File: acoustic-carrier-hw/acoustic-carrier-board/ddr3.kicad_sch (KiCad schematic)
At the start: 21 parts, among them IC1101 MT41K256M16TW-107_P

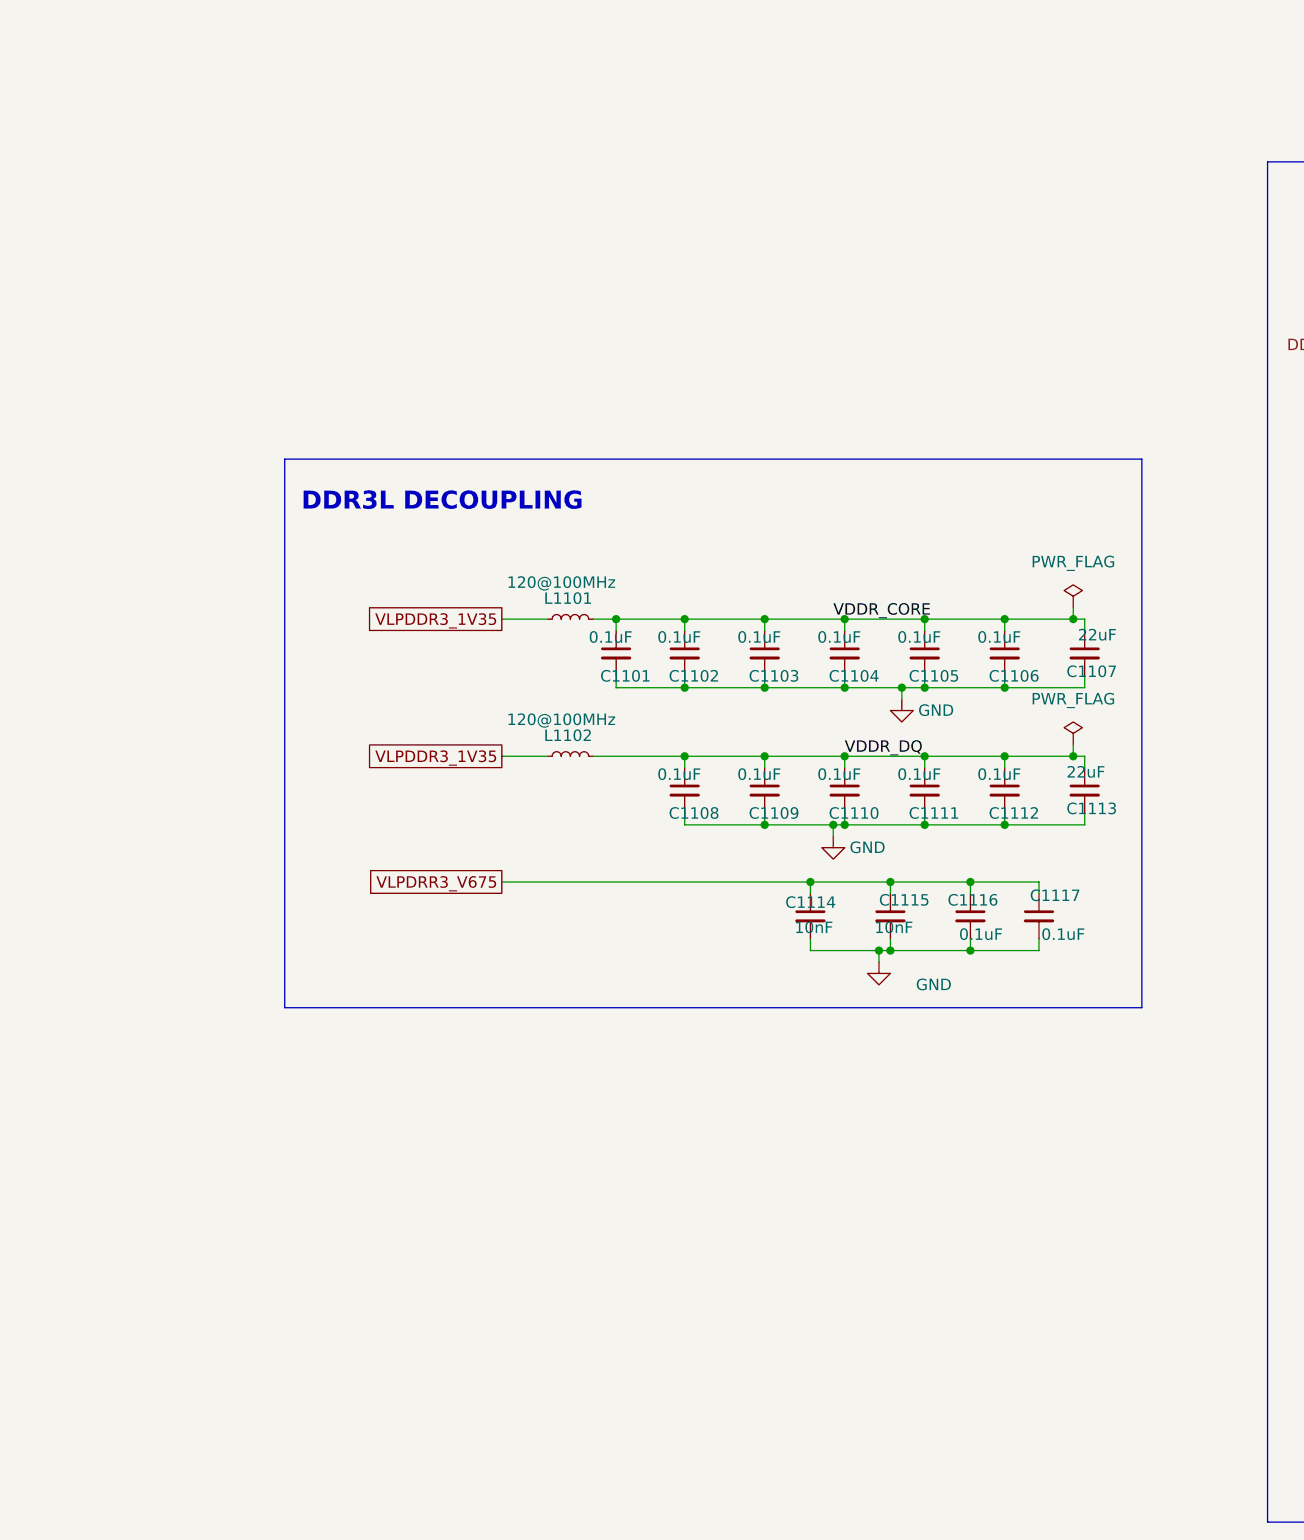
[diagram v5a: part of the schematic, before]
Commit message: [carrier] Removed USB-switch, placed decouplpling for DDR3 and ECP5U (next) consider adding buffers on CC1 and CC2 pins
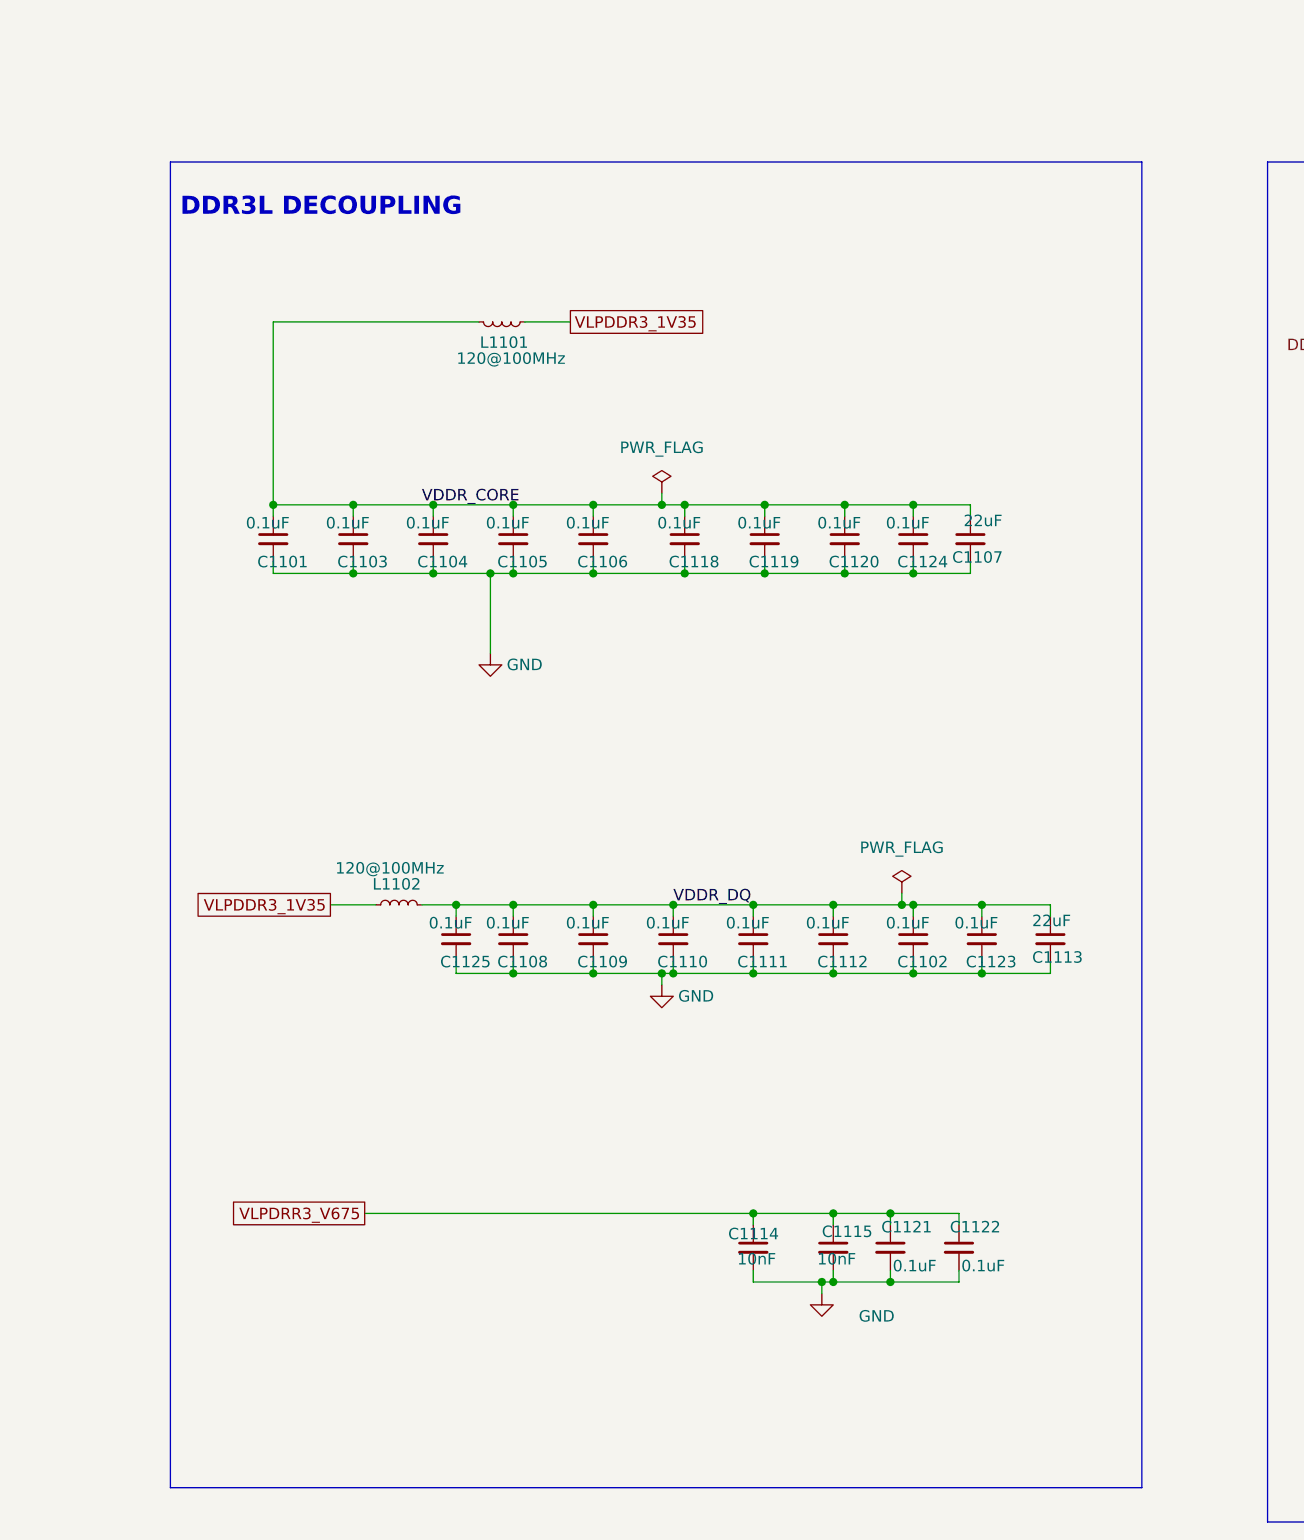
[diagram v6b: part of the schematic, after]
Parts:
- removed C1116, C1117: 0.1uF, Capacitor_SMD:C_0402_1005Metric, symbol Device:C_Small
- added C1118, C1119, C1120, C1121, C1122, C1123, C1124, C1125: 0.1uF, Capacitor_SMD:C_0201_0603Metric, symbol Device:C_Small
- C1101, C1102, C1103, C1104, C1105, C1106, C1108, C1109, C1110, C1111, C1112: footprint Capacitor_SMD:C_0402_1005Metric -> Capacitor_SMD:C_0201_0603Metric; LPN C307331 -> C22435929; MPN CL05B104KB54PNC -> CGA0201X7R104K160ET
- C1114, C1115: footprint Capacitor_SMD:C_0402_1005Metric -> Capacitor_SMD:C_0201_0603Metric; LPN C15195 -> C285010; MPN CL05B103KB5NNNC -> 0201B103K250NT
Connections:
- net GND: now also C1118.2, C1119.2, C1120.2, C1121.2, C1122.2, C1123.2, C1124.2, C1125.2
- net VDDR_CORE: now also C1118.1, C1119.1, C1120.1, C1124.1; no longer C1102.1
- net VDDR_DQ: now also C1102.1, C1123.1, C1125.1
- net VLPDRR3_V675: now also C1121.1, C1122.1
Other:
- moved on the sheet: C1101, C1103, C1104, C1105, C1106, C1107, C1108, C1109, C1110, C1111, C1112, C1113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

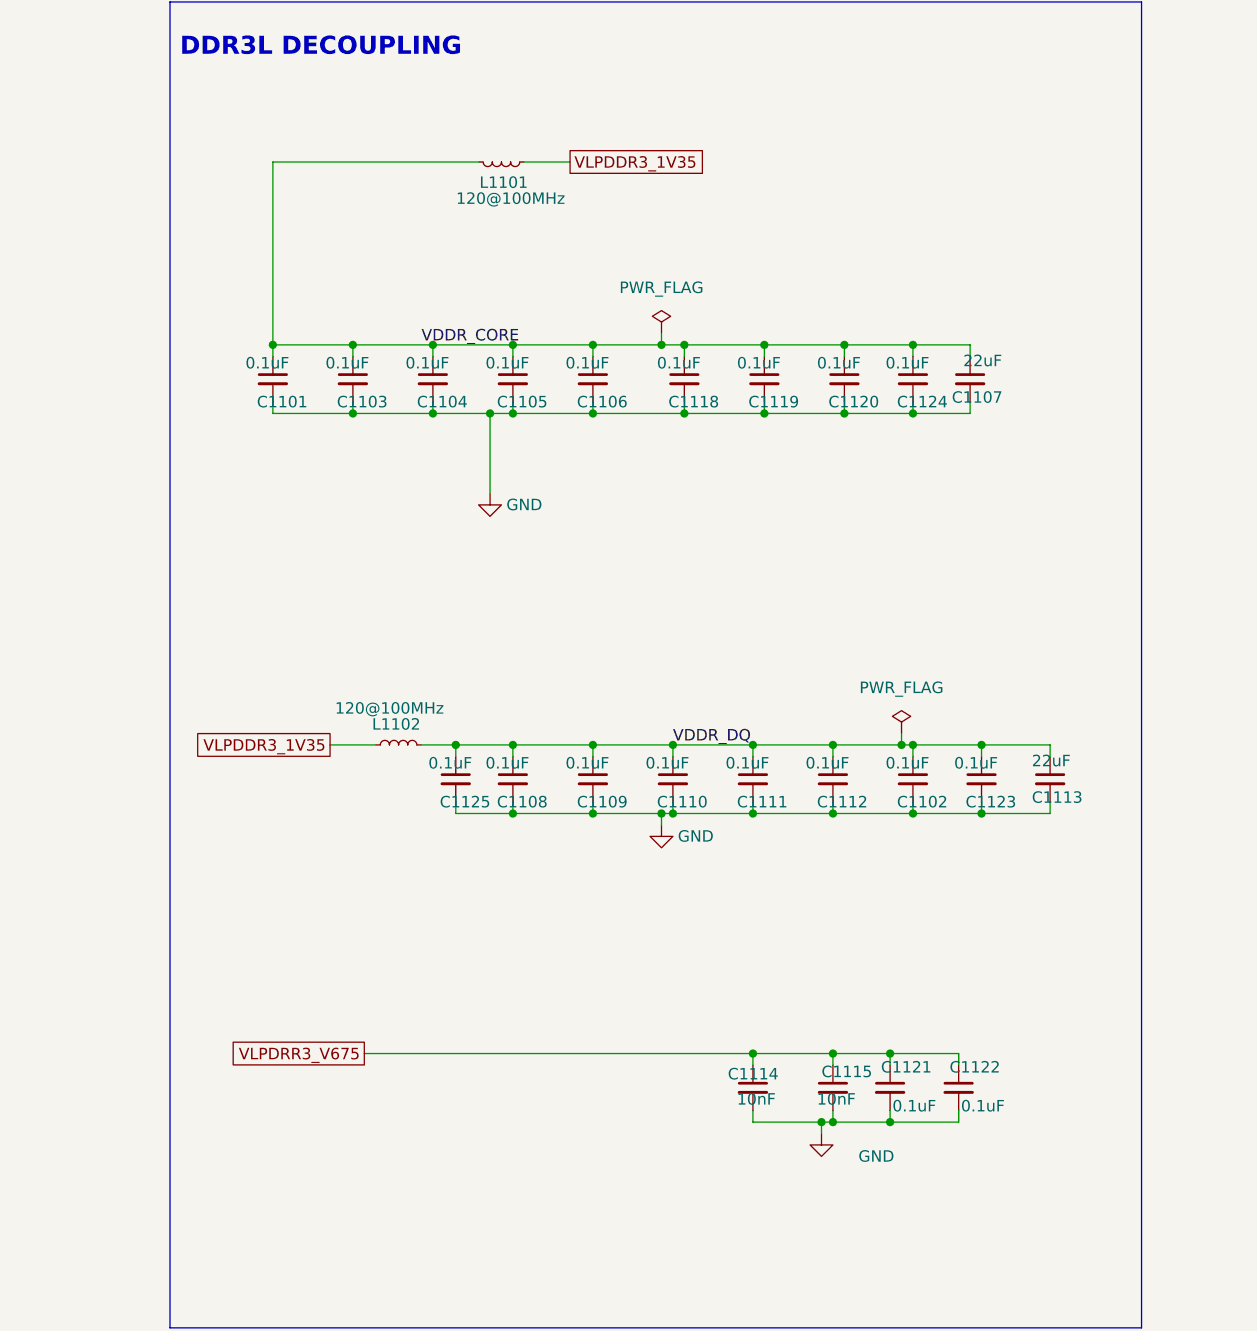
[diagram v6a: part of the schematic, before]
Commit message: [carrier] connected ethernet, usb and adc to appropriate banks, redpositioned schmitt trigger and USB
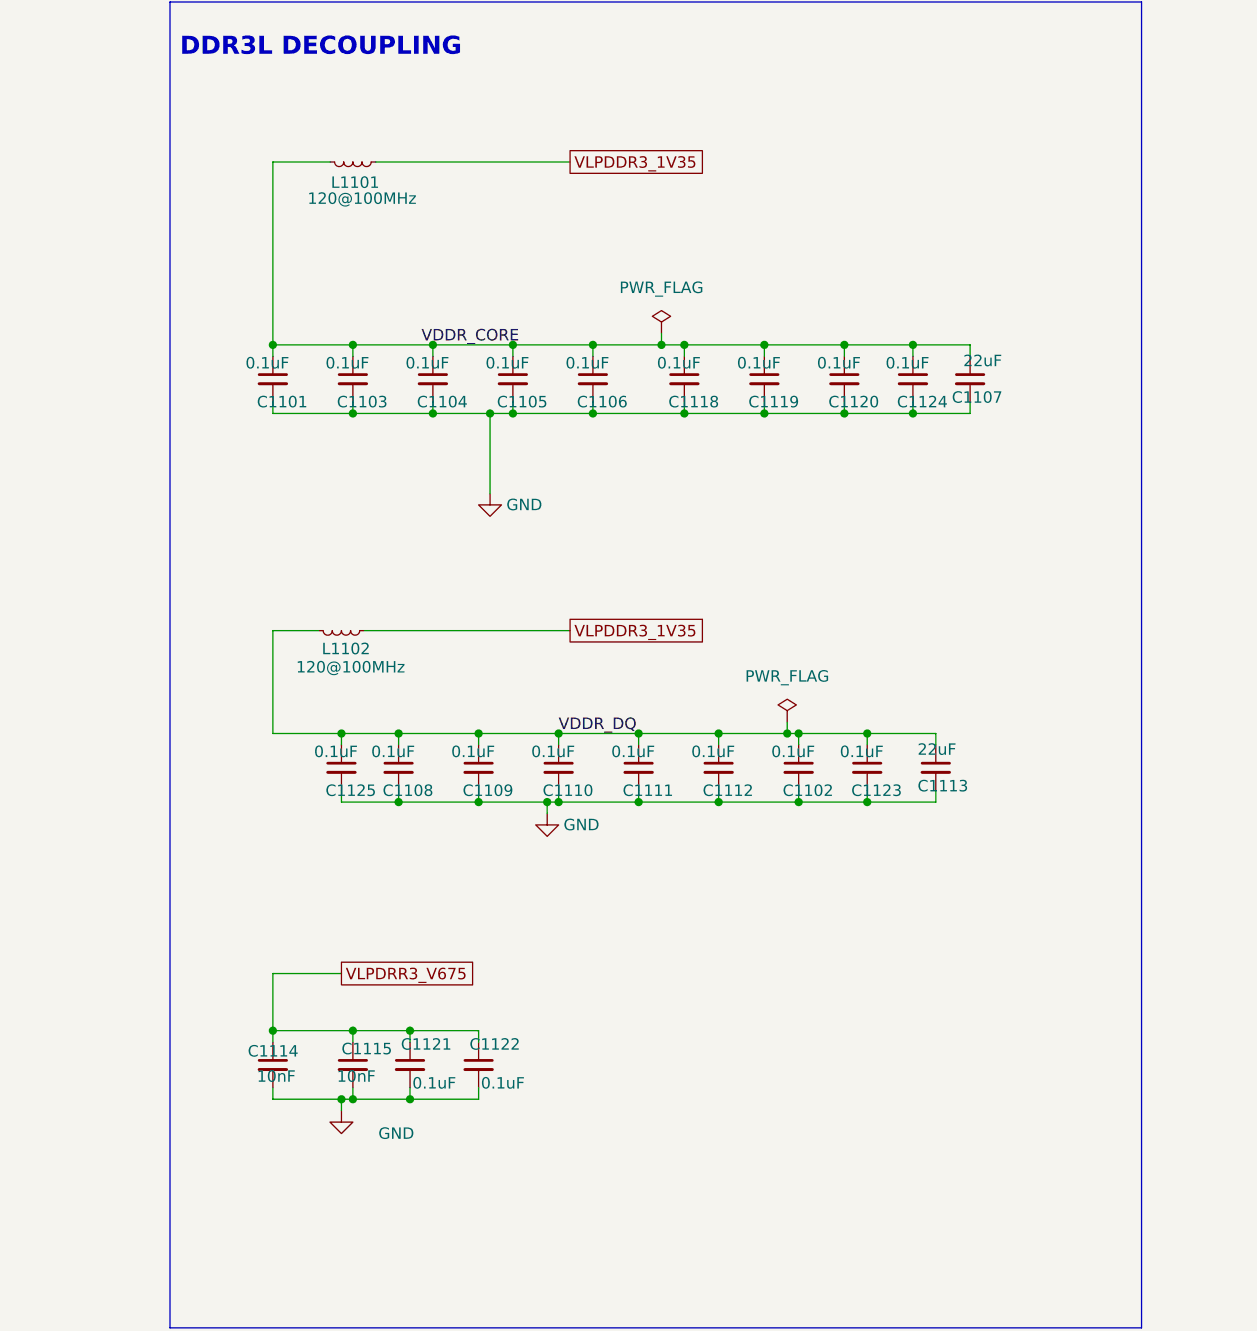
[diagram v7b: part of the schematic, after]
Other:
- moved on the sheet: C1102, C1108, C1109, C1110, C1111, C1112, C1113, C1114, C1115, C1121, C1122, C1123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

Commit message: [carrier] trying horizontal layout
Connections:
- net DDR3.CK renamed DDR3.CK+
- net DDR3.CK# renamed DDR3.CK-
- net DDR3.LDQS renamed DDR3.LDQS+
- net DDR3.LDQS# renamed DDR3.LDQS-
- net DDR3.UDQS renamed DDR3.UDQS-
- net DDR3.UDQS# renamed DDR3.UDQS+
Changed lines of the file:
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@@
 	(bus_alias "LPDDR3_CTL"
 		(members "A[14..0]" "ODT" "CS#" "WE#" "RESET#" "BA[2..0]" "CAS#" "RAS#"
-			"CK" "CK#" "CKE"
+			"CK+" "CK-" "CKE"
 		)
 	)
 	(bus_alias "LPDDR3_DQL"
-		(members "DQ[0..7]" "LDQS" "LDQS#" "LDM")
+		(members "DQ[0..7]" "LDQS+" "LDQS-" "LDM")
 	)
 	(bus_alias "LPDDR3_DQU"
-		(members "DQ[8..15]" "UDQS" "UDQS#" "UDM")
+		(members "DQ[8..15]" "UDQS+" "UDQS-" "UDM")
 	)
 	(rectangle
@@
 		)
 	)
-	(label "DDR3.CK#"
+	(label "DDR3.CK-"
 		(at 261.62 127 0)
 		(effects
@@
 		)
 	)
-	(label "DDR3.LDQS#"
+	(label "DDR3.LDQS-"
 		(at 182.88 87.63 180)
 		(effects
@@
 		)
 	)
-	(label "DDR3.UDQS"
+	(label "DDR3.UDQS-"
 		(at 171.45 55.88 0)
 		(effects
@@
 		)
 	)
-	(label "DDR3.CK"
+	(label "DDR3.CK+"
 		(at 261.62 124.46 0)
 		(effects
@@
 		)
 	)
-	(label "DDR3.UDQS#"
+	(label "DDR3.UDQS+"
 		(at 171.45 53.34 0)
 		(effects
@@
 		)
 	)
-	(label "DDR3.LDQS"
+	(label "DDR3.LDQS+"
 		(at 181.61 85.09 180)
 		(effects
